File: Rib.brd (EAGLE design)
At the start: 127 x 87.6 mm, 34 parts, among them IC1 REG1117, IC2 REG1117, X1 JST-XH-03-PIN-LONG-PAD, X2 JST-XH-03-PIN-LONG-PAD

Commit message: Replaced JST power connectors with screw terminals
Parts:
- removed X1, X2: JST-XH-03-PIN-LONG-PAD, Rembrandt Electronics - JST XH Connectors v1-0:JST-XH-03-PACKAGE-LONG-PAD
- added J1, J2: (no value), SparkFun-Connectors:SCREWTERMINAL-3.5MM-2_LOCK
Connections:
- net GND: now also J1.1, J2.1; no longer X1.1, X2.1
- net N$11: now also J1.2; no longer X1.3
- net N$39: now also J2.2; no longer X2.3
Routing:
- net N$11: track 13.3 -> 14.1 mm
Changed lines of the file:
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@@
 <setting verticaltext="up"/>
 </settings>
-<grid distance="5" unitdist="mil" unit="mil" style="lines" multiple="1" display="yes" altdistance="5" altunitdist="mil" altunit="mil"/>
+<grid distance="1.75" unitdist="mm" unit="mm" style="lines" multiple="1" display="yes" altdistance="5" altunitdist="mil" altunit="mil"/>
 <layers>
 <layer number="1" name="Top" color="4" fill="1" visible="yes" active="yes"/>
@@
 <attribute name="VALUE" x="31.115" y="3.81" size="1.27" layer="27" rot="R90"/>
 </element>
-<element name="X1" library="Rembrandt Electronics - JST XH Connectors v1-0" package="JST-XH-03-PACKAGE-LONG-PAD" value="JST-XH-03-PIN-LONG-PAD" x="0.635" y="68.58" smashed="yes" rot="R180"/>
 <element name="JP2" library="headers" package="1X19" value="" x="-1.905" y="27.94" smashed="yes" rot="R90">
 <attribute name="VALUE" x="1.27" y="3.81" size="1.27" layer="27" rot="R90"/>
@@
 <attribute name="VALUE" x="48.895" y="3.81" size="1.27" layer="27" rot="R90"/>
 </element>
-<element name="X2" library="Rembrandt Electronics - JST XH Connectors v1-0" package="JST-XH-03-PACKAGE-LONG-PAD" value="JST-XH-03-PIN-LONG-PAD" x="64.135" y="67.945" smashed="yes"/>
 <element name="U$3" library="wiichuck" package="CHUCK" value="WIICHUCK" x="89.535" y="71.755" rot="R90"/>
 <element name="U$5" library="wiichuck" package="CHUCK" value="WIICHUCK" x="30.48" y="71.755" rot="R90"/>
@@
 <element name="U$1" library="GF-126-0327" package="GF-126-0327" value="DPDT" x="-8.89" y="59.69"/>
 <element name="U$2" library="GF-126-0327" package="GF-126-0327" value="DPDT" x="59.055" y="59.69"/>
+<element name="J1" library="SparkFun-Connectors" package="SCREWTERMINAL-3.5MM-2_LOCK" value="" x="3.683" y="68.453" rot="R180">
+<attribute name="PROD_ID" value="CONN-08399" x="3.683" y="68.453" size="1.778" layer="27" rot="R180" display="off"/>
+</element>
+<element name="J2" library="SparkFun-Connectors" package="SCREWTERMINAL-3.5MM-2_LOCK" value="" x="65.532" y="68.453" rot="R180">
+<attribute name="PROD_ID" value="CONN-08399" x="65.532" y="68.453" size="1.778" layer="27" rot="R180" display="off"/>
+</element>
 </elements>
 <signals>
@@
 <contactref element="C1" pad="2"/>
 <contactref element="C2" pad="2"/>
-<contactref element="X1" pad="1"/>
-<contactref element="X2" pad="1"/>
 <contactref element="JP16" pad="1"/>
 <contactref element="JP16" pad="24"/>
@@
 <wire x1="32.735" y1="67.505" x2="32.766" y2="67.474" width="0.254" layer="1"/>
 <wire x1="32.766" y1="67.474" x2="32.766" y2="63.119" width="0.254" layer="1"/>
+<contactref element="J1" pad="1"/>
+<contactref element="J2" pad="1"/>
 </signal>
 <signal name="N$7">
@@
 </signal>
 <signal name="N$11">
-<contactref element="X1" pad="3"/>
-<wire x1="-1.905" y1="68.58" x2="-1.905" y2="66.675" width="2.54" layer="1"/>
 <contactref element="U$1" pad="C2"/>
 <contactref element="U$1" pad="C1"/>
-<wire x1="-1.905" y1="66.675" x2="-4.2926" y2="64.2874" width="2.54" layer="1"/>
-<wire x1="-4.2926" y1="64.2874" x2="-4.2926" y2="63.1444" width="2.54" layer="1"/>
+<wire x1="-4.2926" y1="63.1444" x2="-4.2926" y2="64.2874" width="2.54" layer="1"/>
 <wire x1="-4.2926" y1="56.2356" x2="-4.2926" y2="63.1444" width="2.54" layer="16"/>
+<contactref element="J1" pad="2"/>
+<wire x1="-0.127" y1="68.453" x2="0.0052" y2="68.453" width="2.54" layer="1"/>
+<wire x1="-4.2926" y1="64.2874" x2="-0.127" y2="68.453" width="2.54" layer="1"/>
 </signal>
 <signal name="N$39">
-<contactref element="X2" pad="3"/>
 <contactref element="U$2" pad="C2"/>
 <contactref element="U$2" pad="C1"/>
 <wire x1="63.6524" y1="63.1444" x2="63.6524" y2="56.2356" width="2.54" layer="16"/>
-<wire x1="66.675" y1="67.945" x2="66.675" y2="65.405" width="2.54" layer="1"/>
-<wire x1="66.675" y1="65.405" x2="64.4144" y2="63.1444" width="2.54" layer="1"/>
-<wire x1="64.4144" y1="63.1444" x2="63.6524" y2="63.1444" width="2.54" layer="1"/>
+<contactref element="J2" pad="2"/>
+<wire x1="61.8542" y1="68.453" x2="61.8542" y2="64.9426" width="2.54" layer="1"/>
+<wire x1="61.8542" y1="64.9426" x2="63.6524" y2="63.1444" width="2.54" layer="1"/>
 </signal>
 </signals>

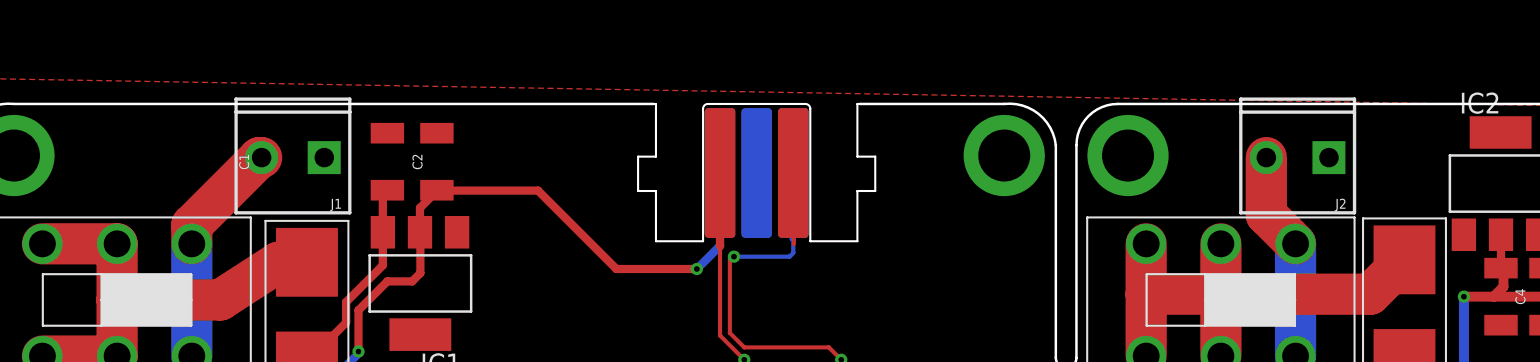
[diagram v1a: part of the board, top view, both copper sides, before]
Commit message: Moved teensy power connector and added solder lugs for a cable to both boards
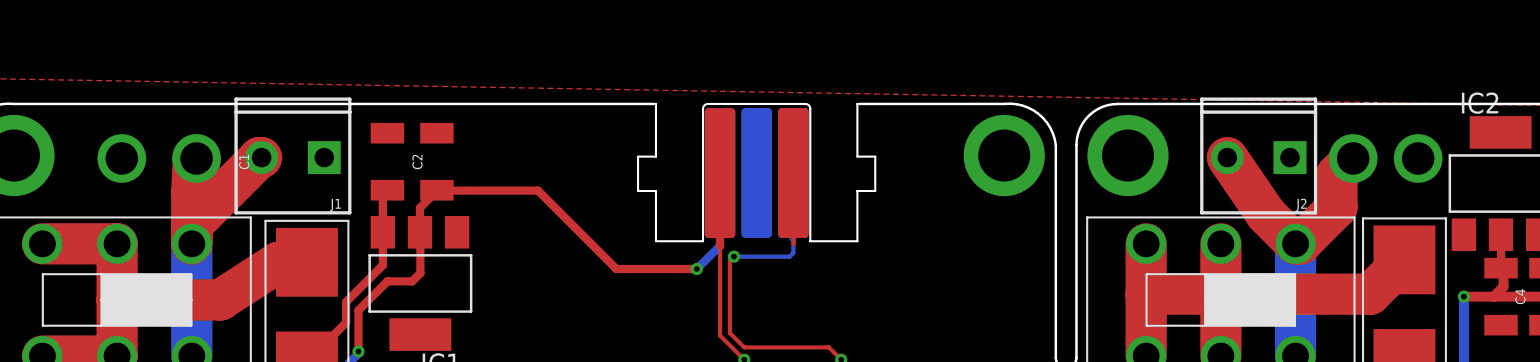
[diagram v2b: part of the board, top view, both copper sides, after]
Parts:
- moved J2 2.40 mm to (63.1, 68.5)
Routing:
- net N$39: track 13.0 -> 20.6 mm, vias 0 -> 1
- net N$11: track 14.1 -> 19.8 mm, vias 0 -> 1
- net GND: vias 29 -> 31
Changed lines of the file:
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@@
 <setting verticaltext="up"/>
 </settings>
-<grid distance="1.75" unitdist="mm" unit="mm" style="lines" multiple="1" display="yes" altdistance="5" altunitdist="mil" altunit="mil"/>
+<grid distance="0.2" unitdist="mm" unit="mm" style="lines" multiple="1" display="yes" altdistance="5" altunitdist="mil" altunit="mil"/>
 <layers>
 <layer number="1" name="Top" color="4" fill="1" visible="yes" active="yes"/>
@@
 <attribute name="PROD_ID" value="CONN-08399" x="3.683" y="68.453" size="1.778" layer="27" rot="R180" display="off"/>
 </element>
-<element name="J2" library="SparkFun-Connectors" package="SCREWTERMINAL-3.5MM-2_LOCK" value="" x="65.532" y="68.453" rot="R180">
-<attribute name="PROD_ID" value="CONN-08399" x="65.532" y="68.453" size="1.778" layer="27" rot="R180" display="off"/>
+<element name="J2" library="SparkFun-Connectors" package="SCREWTERMINAL-3.5MM-2_LOCK" value="" x="63.132" y="68.453" rot="R180">
+<attribute name="PROD_ID" value="CONN-08399" x="63.132" y="68.453" size="1.778" layer="27" rot="R180" display="off"/>
 </element>
 </elements>
@@
 <contactref element="J1" pad="1"/>
 <contactref element="J2" pad="1"/>
+<via x="-8.6" y="68.4" extent="1-16" drill="2"/>
+<via x="71.2" y="68.4" extent="1-16" drill="2"/>
 </signal>
 <signal name="N$7">
@@
 <contactref element="U$1" pad="C2"/>
 <contactref element="U$1" pad="C1"/>
-<wire x1="-4.2926" y1="63.1444" x2="-4.2926" y2="64.2874" width="2.54" layer="1"/>
+<wire x1="-4.2926" y1="64.2874" x2="-4.2926" y2="63.1444" width="2.54" layer="1"/>
 <wire x1="-4.2926" y1="56.2356" x2="-4.2926" y2="63.1444" width="2.54" layer="16"/>
 <contactref element="J1" pad="2"/>
 <wire x1="-0.127" y1="68.453" x2="0.0052" y2="68.453" width="2.54" layer="1"/>
 <wire x1="-4.2926" y1="64.2874" x2="-0.127" y2="68.453" width="2.54" layer="1"/>
+<wire x1="-4.2926" y1="63.1444" x2="-4.2926" y2="66.2926" width="2.54" layer="1"/>
+<wire x1="-4.2926" y1="66.2926" x2="-4.2" y2="68.4" width="2.54" layer="1"/>
+<wire x1="-4.2" y1="68.4" x2="-4" y2="68.4" width="2.54" layer="1"/>
+<via x="-4" y="68.4" extent="1-16" drill="2"/>
+<wire x1="-4" y1="68.4" x2="-3.8" y2="68.2" width="2.54" layer="16"/>
 </signal>
 <signal name="N$39">
@@
 <wire x1="63.6524" y1="63.1444" x2="63.6524" y2="56.2356" width="2.54" layer="16"/>
 <contactref element="J2" pad="2"/>
-<wire x1="61.8542" y1="68.453" x2="61.8542" y2="64.9426" width="2.54" layer="1"/>
+<wire x1="59.4542" y1="68.453" x2="61.8542" y2="64.9426" width="2.54" layer="1"/>
+<via x="67.2" y="68.4" extent="1-16" drill="2"/>
 <wire x1="61.8542" y1="64.9426" x2="63.6524" y2="63.1444" width="2.54" layer="1"/>
+<wire x1="63.6524" y1="63.1444" x2="63.9444" y2="63.1444" width="2.54" layer="1"/>
+<wire x1="63.9444" y1="63.1444" x2="66.2" y2="65.4" width="2.54" layer="1"/>
+<wire x1="66.2" y1="65.4" x2="66.2" y2="67.4" width="2.54" layer="1"/>
+<wire x1="66.2" y1="67.4" x2="67.2" y2="68.4" width="2.54" layer="1"/>
 </signal>
 </signals>

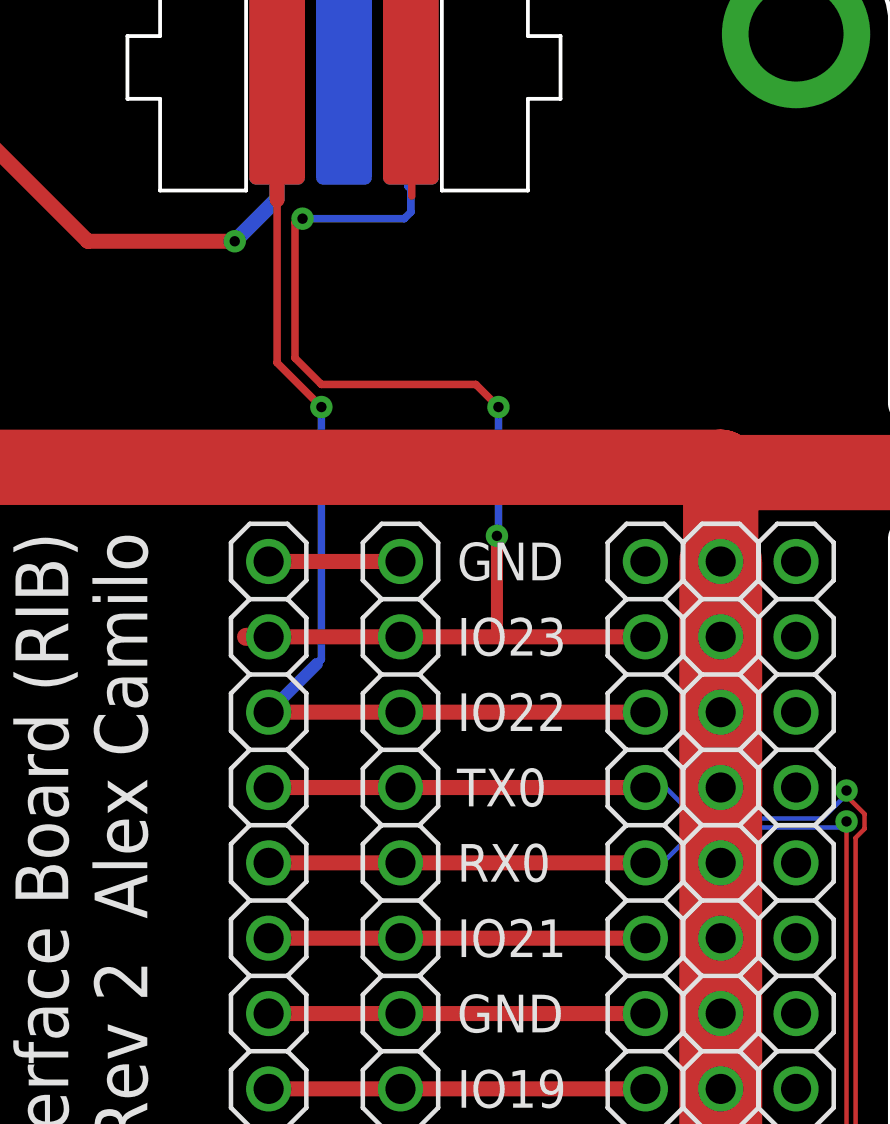
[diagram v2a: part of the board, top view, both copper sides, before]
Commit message: ESP32 SDA now on pin 21
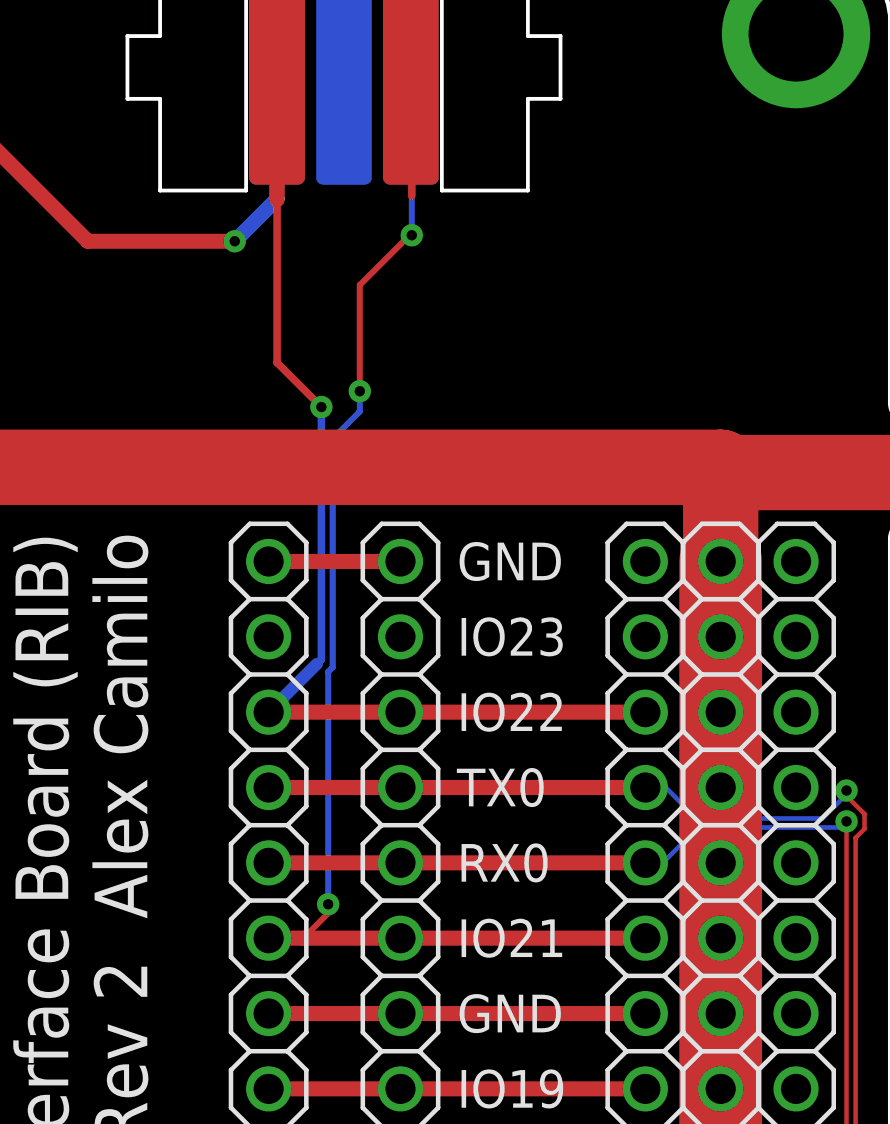
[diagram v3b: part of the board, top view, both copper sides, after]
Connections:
- removed net N$38: JP17.14, JP7.14, JP8.14
- new net N$24: JP17.18, JP7.18, JP8.18
- net SDA: now also JP17.14, JP7.14, JP8.14; no longer JP17.18, JP7.18, JP8.18
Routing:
- net N$38: track 12.7 -> 0.00 mm
- net SDA: track 125.8 -> 128.2 mm
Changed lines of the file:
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@@
 <setting verticaltext="up"/>
 </settings>
-<grid distance="0.2" unitdist="mm" unit="mm" style="lines" multiple="1" display="yes" altdistance="5" altunitdist="mil" altunit="mil"/>
+<grid distance="3" unitdist="mil" unit="mil" style="lines" multiple="1" display="yes" altdistance="5" altunitdist="mil" altunit="mil"/>
 <layers>
 <layer number="1" name="Top" color="4" fill="1" visible="yes" active="yes"/>
@@
 <wire x1="32.385" y1="33.02" x2="27.94" y2="33.02" width="0.508" layer="1"/>
 </signal>
-<signal name="N$38">
-<contactref element="JP8" pad="14"/>
-<contactref element="JP17" pad="14"/>
-<contactref element="JP7" pad="14"/>
-<wire x1="40.64" y1="38.1" x2="32.385" y2="38.1" width="0.508" layer="1"/>
-<wire x1="32.385" y1="38.1" x2="27.94" y2="38.1" width="0.508" layer="1"/>
-</signal>
 <signal name="RX0">
 <contactref element="JP8" pad="15"/>
@@
 <contactref element="U$3" pad="DAT"/>
 <contactref element="U$5" pad="DAT"/>
-<contactref element="JP8" pad="18"/>
-<contactref element="JP17" pad="18"/>
-<contactref element="JP7" pad="18"/>
-<wire x1="35.82038125" y1="48.26" x2="40.64" y2="48.26" width="0.508" layer="1"/>
-<wire x1="35.82038125" y1="48.26" x2="32.385" y2="48.26" width="0.508" layer="1"/>
-<wire x1="32.385" y1="48.26" x2="27.94" y2="48.26" width="0.508" layer="1"/>
-<wire x1="27.94" y1="48.26" x2="27.178" y2="48.26" width="0.6096" layer="1"/>
-<wire x1="35.6362" y1="48.44418125" x2="35.6362" y2="51.6636" width="0.4064" layer="1"/>
-<wire x1="35.6362" y1="48.44418125" x2="35.82038125" y2="48.26" width="0.4064" layer="1"/>
 <contactref element="JP14" pad="9"/>
 <contactref element="JP20" pad="9"/>
@@
 <wire x1="91.79" y1="67.505" x2="91.79" y2="63.5198" width="0.6096" layer="16"/>
 <wire x1="91.79" y1="63.5198" x2="91.694" y2="63.4238" width="0.6096" layer="16"/>
-<via x="35.6362" y="51.6636" extent="1-16" drill="0.35"/>
-<wire x1="35.6362" y1="51.6636" x2="35.687" y2="51.7144" width="0.254" layer="16"/>
-<via x="35.687" y="56.007" extent="1-16" drill="0.35"/>
-<wire x1="35.687" y1="56.007" x2="34.925" y2="56.769" width="0.254" layer="1"/>
-<wire x1="34.925" y1="56.769" x2="29.718" y2="56.769" width="0.254" layer="1"/>
-<wire x1="29.718" y1="56.769" x2="28.829" y2="57.658" width="0.254" layer="1"/>
-<wire x1="28.829" y1="57.658" x2="28.829" y2="62.23" width="0.254" layer="1"/>
-<wire x1="28.829" y1="62.23" x2="28.956" y2="62.357" width="0.254" layer="1"/>
-<wire x1="28.956" y1="62.357" x2="29.083" y2="62.357" width="0.254" layer="1"/>
-<via x="29.083" y="62.357" extent="1-16" drill="0.35"/>
-<wire x1="29.083" y1="62.357" x2="32.512" y2="62.357" width="0.254" layer="16"/>
-<wire x1="32.512" y1="62.357" x2="32.735" y2="62.58" width="0.254" layer="16"/>
-<wire x1="32.735" y1="62.58" x2="32.735" y2="63.3476" width="0.254" layer="16"/>
-<wire x1="35.687" y1="51.7144" x2="35.687" y2="56.007" width="0.254" layer="16"/>
-<wire x1="32.735" y1="63.3476" x2="32.639" y2="63.4436" width="0.254" layer="16"/>
-<wire x1="32.639" y1="63.4436" x2="32.639" y2="63.6016" width="0.254" layer="16"/>
 <wire x1="32.735" y1="67.505" x2="32.766" y2="67.474" width="0.254" layer="16"/>
 <wire x1="32.766" y1="67.474" x2="32.766" y2="66.929" width="0.254" layer="16"/>
 <wire x1="32.766" y1="66.929" x2="32.639" y2="66.802" width="0.254" layer="16"/>
 <wire x1="32.639" y1="66.802" x2="32.639" y2="65.786" width="0.254" layer="16"/>
-<wire x1="32.639" y1="63.6016" x2="32.639" y2="65.786" width="0" layer="19" extent="16-16"/>
-<wire x1="75.692" y1="50.5968" x2="40.64" y2="48.26" width="0" layer="19" extent="1-1"/>
+<contactref element="JP8" pad="14"/>
+<contactref element="JP17" pad="14"/>
+<contactref element="JP7" pad="14"/>
+<wire x1="40.64" y1="38.1" x2="32.385" y2="38.1" width="0.508" layer="1"/>
+<wire x1="32.385" y1="38.1" x2="29.1084" y2="38.1" width="0.508" layer="1"/>
+<wire x1="29.1084" y1="38.1" x2="27.94" y2="38.1" width="0.508" layer="1"/>
+<wire x1="27.94" y1="38.1" x2="29.1" y2="38.1" width="0.1524" layer="1"/>
+<wire x1="29.1084" y1="38.1" x2="29.1084" y2="38.1084" width="0.2032" layer="1"/>
+<wire x1="29.1084" y1="38.1" x2="29.9466" y2="38.9382" width="0.2032" layer="1"/>
+<wire x1="29.9466" y1="38.9382" x2="29.9466" y2="39.243" width="0.2032" layer="1"/>
+<via x="29.9466" y="39.243" extent="1-16" drill="0.35"/>
+<wire x1="29.9466" y1="39.243" x2="29.9466" y2="47.08001875" width="0.2032" layer="16"/>
+<wire x1="30.099" y1="54.9402" x2="31.0134" y2="55.8546" width="0.2032" layer="16"/>
+<wire x1="29.9466" y1="47.08001875" x2="30.099" y2="47.23241875" width="0.2032" layer="16"/>
+<wire x1="30.099" y1="47.23241875" x2="30.099" y2="54.9402" width="0.2032" layer="16"/>
+<via x="31.0134" y="56.5404" extent="1-16" drill="0.35"/>
+<wire x1="31.0134" y1="56.5404" x2="31.0134" y2="60.1218" width="0.2032" layer="1"/>
+<wire x1="31.0134" y1="60.1218" x2="32.6136" y2="61.722" width="0.2032" layer="1"/>
+<wire x1="32.6136" y1="61.722" x2="32.766" y2="61.7982" width="0.2032" layer="1"/>
+<via x="32.766" y="61.7982" extent="1-16" drill="0.35"/>
+<wire x1="32.766" y1="61.7982" x2="32.766" y2="63.627" width="0.2032" layer="16"/>
+<wire x1="31.0134" y1="55.8546" x2="31.0134" y2="56.5404" width="0.2032" layer="16"/>
+<wire x1="32.766" y1="63.627" x2="32.639" y2="65.786" width="0" layer="19" extent="16-16"/>
+<wire x1="58.42" y1="12.7" x2="40.64" y2="38.1" width="0" layer="19" extent="1-1"/>
 <wire x1="68.58" y1="12.7" x2="73.025" y2="12.7" width="0" layer="19" extent="1-1"/>
 </signal>
@@
 <wire x1="66.2" y1="67.4" x2="67.2" y2="68.4" width="2.54" layer="1"/>
 </signal>
+<signal name="N$24">
+<contactref element="JP17" pad="18"/>
+<contactref element="JP8" pad="18"/>
+<contactref element="JP7" pad="18"/>
+<wire x1="32.385" y1="48.26" x2="40.64" y2="48.26" width="0" layer="19" extent="1-1"/>
+<wire x1="27.94" y1="48.26" x2="32.385" y2="48.26" width="0" layer="19" extent="1-1"/>
+</signal>
 </signals>
